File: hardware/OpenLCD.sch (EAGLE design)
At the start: 32 parts, among them Q1 PNP, Q2 PNP, Q3 PNP, U1 MIC5219, U2 ATMEGA328P_TQFP, Y1 8MHz

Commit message: Board layout complete
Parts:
- removed C2, C5: 22pF, SparkFun-Capacitors:22PF-50V-5%(0603)
- removed JP16: (no value), SparkFun-Connectors:M06SIP_LOCK
- removed JP17: (no value), SparkFun-Connectors:M08LOCK
- removed JP8: RESET, SparkFun-Connectors:M01PTH
- removed JP9: JST, SparkFun-Connectors:M03JST-SMD
- removed SJ3, SJ4: JUMPER-PAD-3-2OF3_NC_BY_PASTE, SparkFun-Passives:JUMPER-PAD-3-2OF3_NC_BY_PASTE
- removed Y1: 8MHz, SparkFun-FreqCtrl:CRYSTAL5X3
- added JP3: JST, SparkFun-Connectors:M03JST-SMD
- added JP4: (no value), SparkFun-Connectors:M08LOCK
- added JP5: (no value), SparkFun-Connectors:M06SIP_LOCK
- added JP6: RESET, SparkFun-Connectors:M01PTH
- added R3: 10K, SparkFun-Resistors:10KOHM-1/10W-1%(0603)0603
- added SJ1, SJ2: JUMPER-PAD-3-2OF3_NC_BY_PASTE, SparkFun-Passives:JUMPER-PAD-3-2OF3_NC_BY_PASTE
- added Y2: 8MHz, SparkFun-FreqCtrl:RESONATOR8MHZ
- C13, C19: device SparkFun:CAP_POL1206 -> SparkFun-Capacitors:10UF-16V-10%(TANT)
- JP2: device SparkFun-Connectors:M10" -> SparkFun-Connectors:M10SILK_FEMALE_PTH
- Q1, Q2, Q3: value PNP -> PNP-500mA; device SparkFun-DiscreteSemi:TRANSISTOR_PNPSMD -> SparkFun-DiscreteSemi:TRANSISTOR-PNP-DDTB142TC
- U1: value MIC5219 -> ATMEGA328P_TQFP; device SparkFun:V_REG_LDOSMD -> SparkFun-DigitalIC:ATMEGA328P_TQFP
- U2: value ATMEGA328P_TQFP -> MIC5219; device SparkFun-DigitalIC:ATMEGA328P_TQFP -> SparkFun-PowerIC:V_REG_MIC52195V
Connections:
- removed net E: JP16.1, U2.PC2(ADC2)
- new net EN: JP5.1, U1.PC2(ADC2)
- net !SS: now also R3.1, U1.PB2(SS/OC1B); no longer U2.PB2(SS/OC1B)
- net A-BLUE: now also JP4.1; no longer JP17.1
- net A-GREEN: now also JP4.2; no longer JP17.2
- net A-RED/WHITE: now also SJ1.1, SJ2.3; no longer SJ3.3, SJ4.1
- net A6: now also U1.ADC6; no longer U2.ADC6
- net A7: now also U1.ADC7; no longer U2.ADC7
- net AREF: now also U1.AREF; no longer U2.AREF
- net BACKLIGHT1: now also JP4.4, SJ2.2; no longer JP17.4, SJ3.2
- net BACKLIGHT2: now also JP4.3, SJ1.2; no longer JP17.3, SJ4.2
- net BL-B: now also U1.PB1(OC1A); no longer U2.PB1(OC1A)
- net BL-G: now also U1.PD6(AIN0); no longer U2.PD6(AIN0)
- net BL-R/W: now also U1.PD5(T1); no longer U2.PD5(T1)
- net CONTRAST: now also JP5.4; no longer JP16.4
- net D4: now also JP4.8, U1.PC3(ADC3); no longer JP17.8, U2.PC3(ADC3)
- net D5: now also JP4.7, U1.PD2(INT0); no longer JP17.7, U2.PD2(INT0)
- net D6: now also JP4.6, U1.PD3(INT1); no longer JP17.6, U2.PD3(INT1)
- net D7: now also JP4.5, U1.PD4(XCK/T0); no longer JP17.5, U2.PD4(XCK/T0)
- net GND: now also JP3.2, JP5.6, SJ1.3, SJ2.1, U1.AGND, U1.GND@3, U1.GND@5, U2.GND, Y2.2; no longer C2.1, C5.1, JP16.6, JP9.2, SJ3.1, SJ4.3, U1.GND, U2.AGND, U2.GND@3, U2.GND@5
- net N$2: now also U1.PB7(XTAL2/TOSC2), Y2.3; no longer C2.2, U2.PB6(XTAL1/TOSC1), Y1.2
- net N$3: now also U1.PB6(XTAL1/TOSC1), Y2.1; no longer C5.2, U2.PB7(XTAL2/TOSC2), Y1.1
- net R/W: now also JP5.2, U1.PC1(ADC1); no longer JP16.2, U2.PC1(ADC1)
- net RAW: now also JP3.1, U2.EN, U2.IN; no longer JP9.1, U1.EN, U1.IN
- net RS: now also JP5.3, U1.PC0(ADC0); no longer JP16.3, U2.PC0(ADC0)
- net RST: now also JP6.1, U1.PC6(/RESET); no longer JP8.1, U2.PC6(/RESET)
- net RXI: now also JP3.3, U1.PD0(RXD); no longer JP9.3, U2.PD0(RXD)
- net SCK: now also U1.PB5(SCK); no longer U2.PB5(SCK)
- net SCL: now also U1.PC5(ADC5/SCL); no longer U2.PC5(ADC5/SCL)
- net SDA: now also U1.PC4(ADC4/SDA); no longer U2.PC4(ADC4/SDA)
- net SDI: now also U1.PB3(MOSI/OC2); no longer U2.PB3(MOSI/OC2)
- net SDO: now also U1.PB4(MISO); no longer U2.PB4(MISO)
- net TXO: now also U1.PD1(TXD); no longer U2.PD1(TXD)
- net VCC: now also JP5.5, R3.2, U1.AVCC, U1.VCC@4, U1.VCC@6, U2.OUT; no longer JP16.5, U1.OUT, U2.AVCC, U2.VCC@4, U2.VCC@6
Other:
- note added: "7-bit I2C Address: 0x72"
- note added: "SPI Pull-Up"
- note removed: "Do we want I2C adr jumpers? 2 IO + GND jumper = 4 settings."
- note removed: "Do we want meter and counter mode jumpers?"
- note removed: "Should we have jumper to select 5V/3.3V?"
- moved on the sheet: C1, C13, C19, C3, C4, JP1, JP2, R1, R2, R5, R6, R7

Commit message: Adding jumpers for size and voltage.
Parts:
- removed C13, C19: 10uF, SparkFun-Capacitors:10UF-16V-10%(TANT)
- removed U2: MIC5219, SparkFun-PowerIC:V_REG_MIC52195V
- added C2: 1.0uF/25V, SparkFun-Capacitors:1.0UF-25V-+80/-20(0805)
- added C6: 2.2uF, SparkFun-Capacitors:2.2UF-10V-20%(0603)
- added R4: 330, SparkFun-Resistors:330OHM1/10W1%(0603)
- added R8: 240, SparkFun-Resistors:240OHM1/10W1%(0603)
- added R9: 390, SparkFun-Resistors:390OHM1/10W1%(0603)
- added SJ3: VSET, SparkFun-Passives:JUMPER-PAD-2-NOYES_SILK
- added SJ5: Size, SparkFun-Passives:JUMPER-PAD-2-NOYES_SILK
- added U3: MIC5205-ADJ, SparkFun-PowerIC:V_REG_MIC5205ADJ
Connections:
- removed net A6: U1.ADC6
- removed net A7: U1.ADC7
- new net N$6: R8.1, R9.2, U3.BP
- new net N$7: R4.2, R9.1, SJ3.2
- new net SIZE: SJ5.2, U1.PD7(AIN1)
- net GND: now also C2.2, C6.2, R4.1, SJ3.1, SJ5.1, U3.GND; no longer C13.-, C19.-, U2.GND
- net RAW: now also C2.1, U3.EN, U3.IN; no longer C19.+, U2.EN, U2.IN
- net VCC: now also C6.1, R8.2, U3.OUT; no longer C13.+, U2.OUT
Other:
- note added: "Default: Open for 16x2 Close jumper to set LCD to 20x4 Can be overwritten in software"
- note added: "Default: Open for 5V Close jumper for 3.3V"
- note removed: "1 for counter"
- note removed: "Add OSHW logo"
- note removed: "Add silk to top side A6/7"
- note removed: "Board is marked with voltage."
- note removed: "Changed SPI pins to SDO/SDI to match"
- note removed: "Ganged I2C + pwr"
- note removed: "Move in 10uF cap"
- note removed: "Silkscreen squares for colors"
- note removed: "VCC may be 3.3V or 5V"
- note removed: "original S7S"
- moved on the sheet: C1, C3, C4, JP1, JP6, R1, R3, U1, Y2

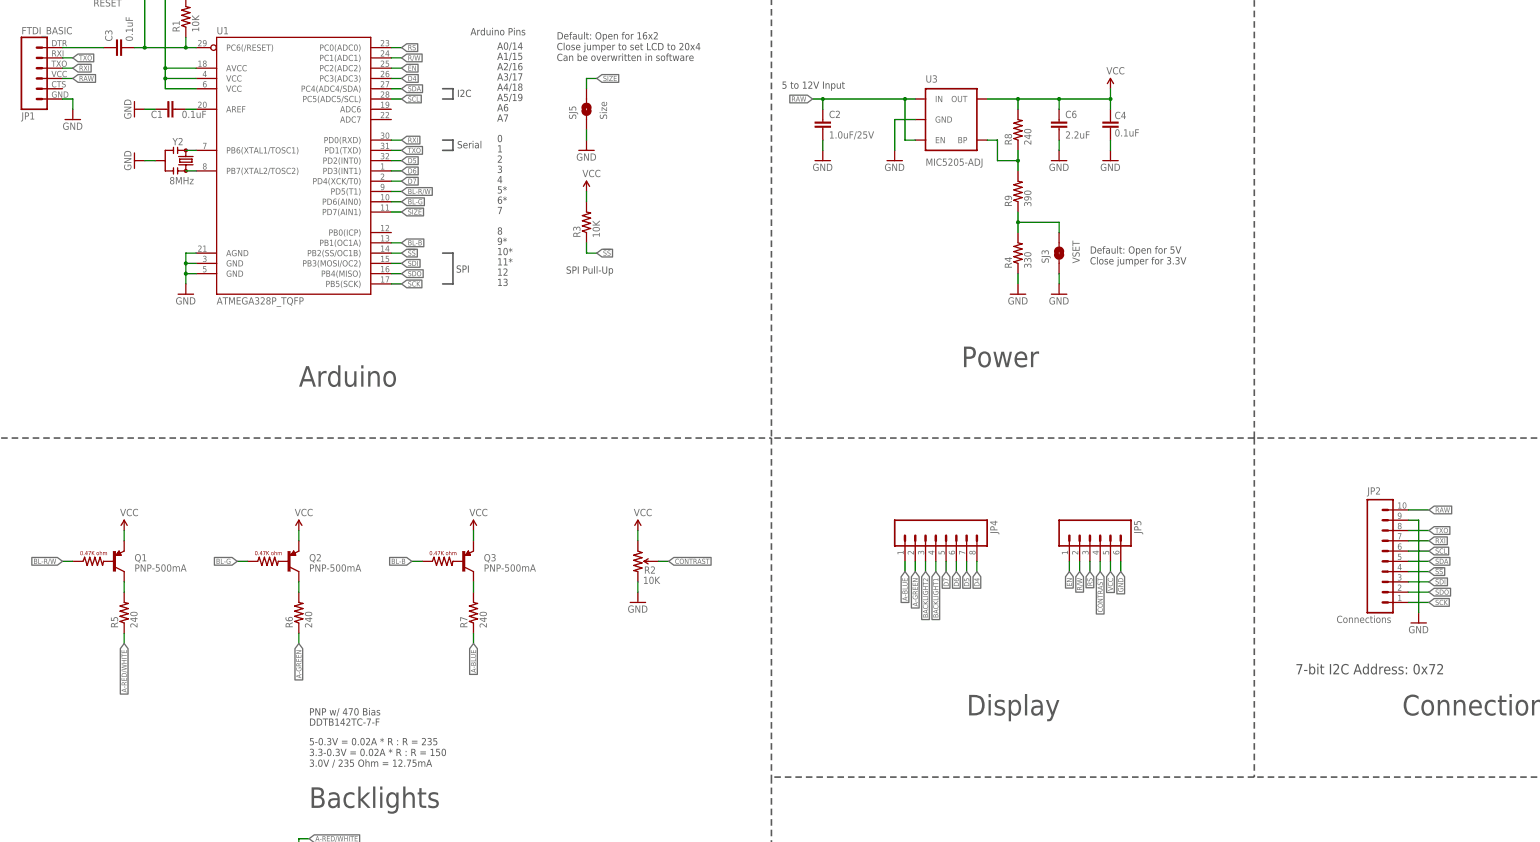
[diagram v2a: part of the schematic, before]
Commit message: Standard I2C interface. I2C pull ups. VCC on FTDI connector.
Added silk to both sides. Moved contrast pin to PWM pin and direct
connect.
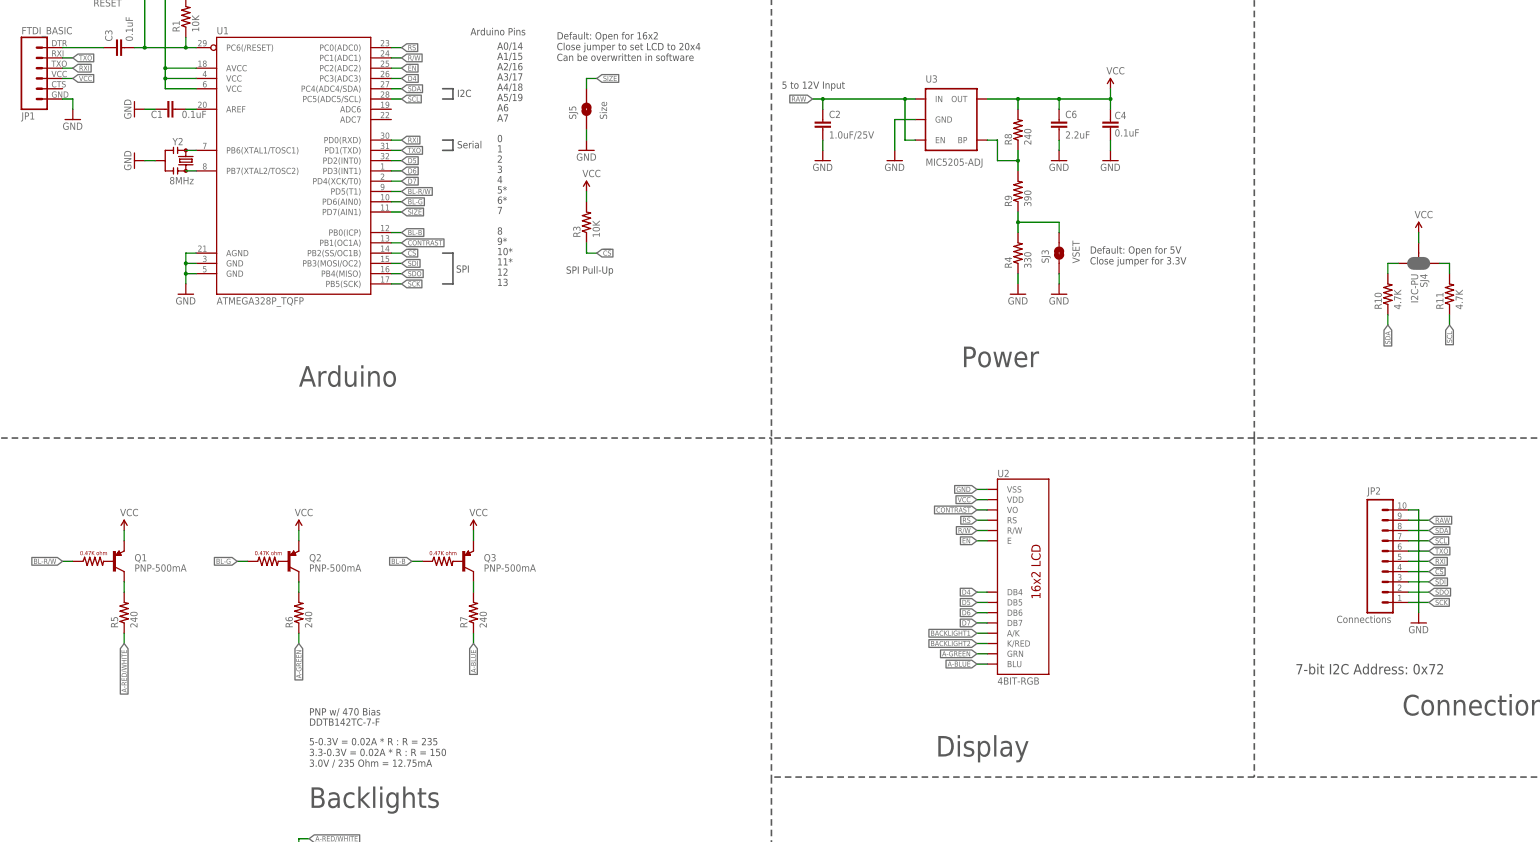
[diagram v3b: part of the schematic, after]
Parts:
- removed JP4: (no value), SparkFun-Connectors:M08LOCK
- removed JP5: (no value), SparkFun-Connectors:M06SIP_LOCK
- removed R2: 10K, SparkFun-Electromechanical:TRIMPOT3MM-2
- added R10, R11: 4.7K, SparkFun-Resistors:4.7KOHM-1/10W-1%(0603)
- added SJ4: I2C-PU, SparkFun-Passives:JUMPER-PAD-3-NC_BY_PASTE
- added U2: 4BIT-RGB, SparkFun-Displays:LCD-16X2-MINMIN4-RGB
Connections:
- net !SS renamed !CS
- new net N$10: R10.2, SJ4.3
- new net N$9: R11.2, SJ4.1
- net A-BLUE: now also U2.BLU; no longer JP4.1
- net A-GREEN: now also U2.GRN; no longer JP4.2
- net BACKLIGHT1: now also U2.A/K; no longer JP4.4
- net BACKLIGHT2: now also U2.K/RED; no longer JP4.3
- net BL-B: now also U1.PB0(ICP); no longer U1.PB1(OC1A)
- net CONTRAST: now also U1.PB1(OC1A), U2.VO; no longer JP5.4, R2.WIPER
- net D4: now also U2.DB4; no longer JP4.8
- net D5: now also U2.DB5; no longer JP4.7
- net D6: now also U2.DB6; no longer JP4.6
- net D7: now also U2.DB7; no longer JP4.5
- net EN: now also U2.E; no longer JP5.1
- net GND: now also JP2.10, U2.VSS; no longer JP2.9, JP5.6, R2.CW
- net R/W: now also U2.R/W; no longer JP5.2
- net RAW: now also JP2.9; no longer JP1.4, JP2.10
- net RS: now also U2.RS; no longer JP5.3
- net RXI: now also JP2.5; no longer JP2.7
- net SCL: now also JP2.7, R11.1; no longer JP2.6
- net SDA: now also JP2.8, R10.1; no longer JP2.5
- net TXO: now also JP2.6; no longer JP2.8
- net VCC: now also JP1.4, SJ4.2, U2.VDD; no longer JP5.5, R2.CCW

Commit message: Final touchup before QC review.
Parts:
- SJ3: value VSET -> 3.3V
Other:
- note added: "Default: Closed Open jumper to remove I2C pull up resistors from bus"
- note added: "In general 5V to 12V is allowed"
- note added: "It is recommended that the minimum input voltage is 0.15V more than board operating voltage."
- note added: "Jumpers and Pullups"
- note added: "N. Seidle"
- note added: "v01"
- moved on the sheet: C1, C2, C3, C4, C6, JP1, JP6, Q1, Q2, Q3, R1, R10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

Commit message: Resolved issue 1
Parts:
- added TP1, TP2: TEST-POINT3X4, SparkFun-Passives:TEST-POINT3X4
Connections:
- net GND: now also JP1.5
- net N$7: now also TP1.1
- net SIZE: now also TP2.1
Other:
- moved on the sheet: SJ1
